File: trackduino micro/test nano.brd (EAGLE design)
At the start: 43.4 x 19.1 mm, 25 parts, among them IC2 74AHC1G125DBV, SW1 SPST_TACT-KMR2, U1 ATMEGA168MLF, X1 SMA-SMD, Y1 16MHZ

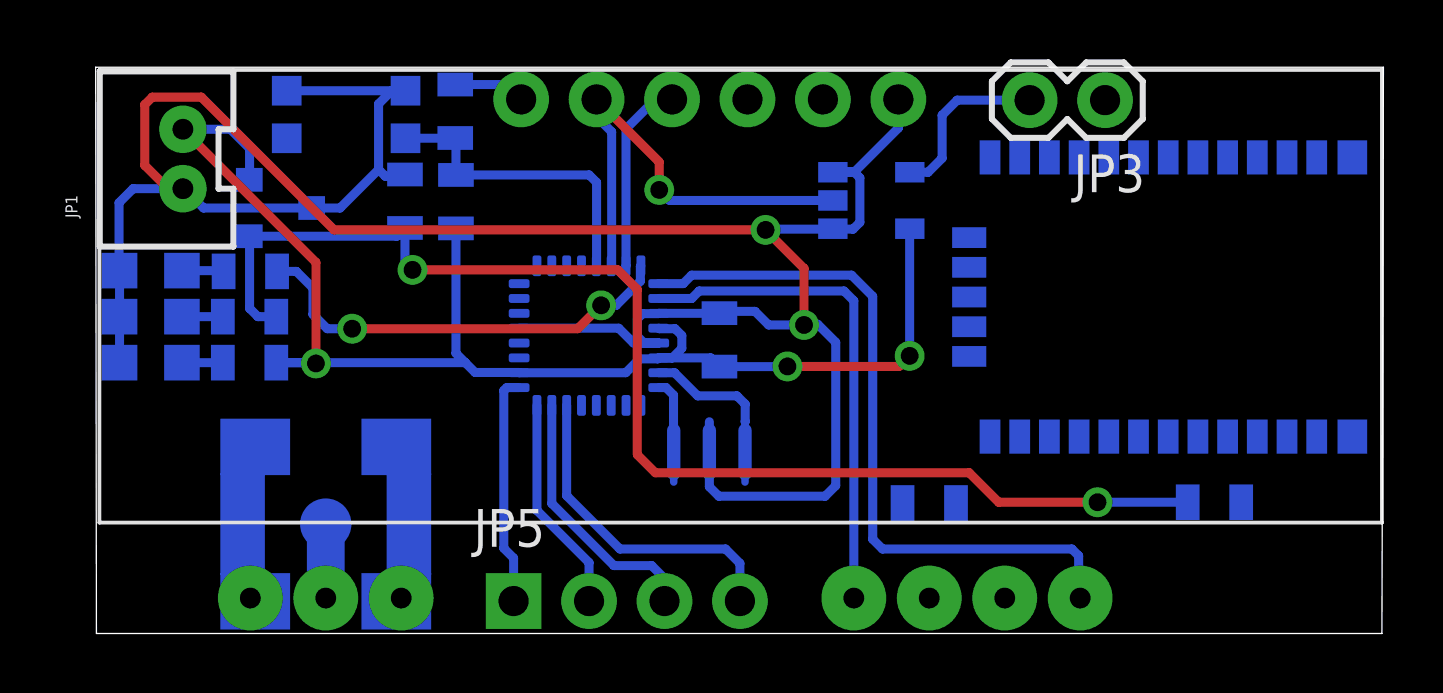
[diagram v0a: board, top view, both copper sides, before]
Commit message: minor fixes to smallest boards
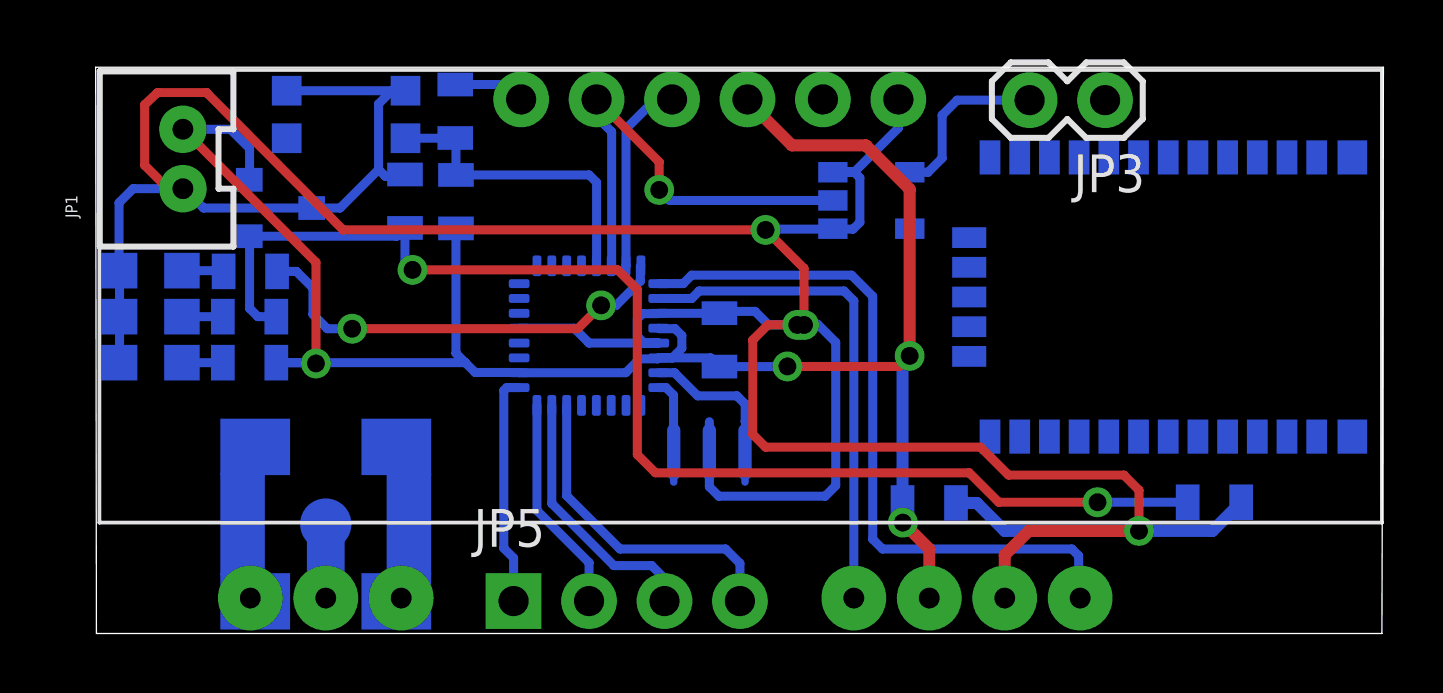
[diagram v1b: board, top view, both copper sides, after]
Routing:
- net GND: track 88.4 -> 125.2 mm, vias 2 -> 4
- net VCC: track 47.8 -> 68.7 mm, vias 3 -> 4
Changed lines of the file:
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@@
 <wire x1="76.8604" y1="71.0692" x2="76.1952" y2="71.0692" width="0.3048" layer="16"/>
 <wire x1="76.1952" y1="71.0692" x2="76.18" y2="71.0844" width="0.3048" layer="16"/>
-<wire x1="65.61656875" y1="67.734715625" x2="68.968084375" y2="67.734715625" width="0.3048" layer="16"/>
-<wire x1="68.968084375" y1="67.734715625" x2="69.469" y2="67.2338" width="0.3048" layer="16"/>
-<wire x1="69.469" y1="67.2338" x2="70.315653125" y2="67.2338" width="0.3048" layer="16"/>
+<wire x1="65.61656875" y1="67.734715625" x2="67.469484375" y2="67.734715625" width="0.3048" layer="16"/>
+<wire x1="67.469484375" y1="67.734715625" x2="67.9704" y2="67.2338" width="0.3048" layer="16"/>
+<wire x1="67.9704" y1="67.2338" x2="70.315653125" y2="67.2338" width="0.3048" layer="16"/>
 <wire x1="70.315653125" y1="67.2338" x2="70.31656875" y2="67.234715625" width="0.3048" layer="16"/>
 <wire x1="70.31656875" y1="67.234715625" x2="69.823684375" y2="67.234715625" width="0.3048" layer="16"/>
@@
 <wire x1="76.2762" y1="62.4332" x2="76.2762" y2="67.2592" width="0.3048" layer="16"/>
 <wire x1="76.2762" y1="67.2592" x2="75.6666" y2="67.8688" width="0.3048" layer="16"/>
-<wire x1="75.2094" y1="67.8434" x2="74.0156" y2="67.8434" width="0.3048" layer="16"/>
+<wire x1="75.2094" y1="67.8434" x2="74.9808" y2="67.8434" width="0.3048" layer="16"/>
+<wire x1="74.9808" y1="67.8434" x2="74.0156" y2="67.8434" width="0.3048" layer="16"/>
 <wire x1="74.0156" y1="67.8434" x2="73.5584" y2="68.3006" width="0.3048" layer="16"/>
 <wire x1="73.5584" y1="68.3006" x2="72.420778125" y2="68.3006" width="0.3048" layer="16"/>
@@
 <wire x1="73.9394" y1="71.0692" x2="73.914" y2="71.0438" width="0.3048" layer="16"/>
 <via x="73.914" y="71.0438" extent="1-16" drill="0.6" shape="square"/>
-<wire x1="73.914" y1="71.0438" x2="59.3852" y2="71.0438" width="0.3048" layer="1"/>
-<wire x1="59.3852" y1="71.0438" x2="54.9148" y2="75.5142" width="0.3048" layer="1"/>
-<wire x1="54.9148" y1="75.5142" x2="53.2638" y2="75.5142" width="0.3048" layer="1"/>
-<wire x1="53.2638" y1="75.5142" x2="53.0098" y2="75.2602" width="0.3048" layer="1"/>
+<wire x1="73.914" y1="71.0438" x2="59.69" y2="71.0438" width="0.3048" layer="1"/>
+<wire x1="59.69" y1="71.0438" x2="55.0926" y2="75.6666" width="0.3048" layer="1"/>
+<wire x1="55.0926" y1="75.6666" x2="53.4416" y2="75.6666" width="0.3048" layer="1"/>
+<wire x1="53.4416" y1="75.6666" x2="53.0098" y2="75.2602" width="0.3048" layer="1"/>
 <wire x1="53.0098" y1="75.2602" x2="53.0098" y2="73.2188" width="0.3048" layer="1"/>
 <wire x1="53.0098" y1="73.2188" x2="53.7972" y2="72.4314" width="0.3048" layer="1"/>
@@
 <wire x1="75.2094" y1="67.8434" x2="75.2094" y2="69.7484" width="0.3048" layer="1"/>
 <wire x1="75.2094" y1="69.7484" x2="73.914" y2="71.0438" width="0.3048" layer="1"/>
-<wire x1="81.9658" y1="58.6486" x2="89.927" y2="61.8744" width="0" layer="19" extent="16-16"/>
-<wire x1="80.3258" y1="61.849" x2="81.9658" y2="58.6486" width="0" layer="19" extent="16-16"/>
-<wire x1="76.2762" y1="62.4332" x2="80.3258" y2="61.849" width="0" layer="19" extent="16-16"/>
-<wire x1="56.7308" y1="63.7378" x2="52.163" y2="66.5734" width="0" layer="19" extent="16-16"/>
+<wire x1="80.3258" y1="61.849" x2="81.026" y2="61.849" width="0.4064" layer="16"/>
+<wire x1="81.026" y1="61.849" x2="81.9658" y2="60.9092" width="0.4064" layer="16"/>
+<wire x1="81.9658" y1="60.9092" x2="86.487" y2="60.9092" width="0.4064" layer="16"/>
+<wire x1="81.9658" y1="58.6486" x2="81.9658" y2="60.0964" width="0.4064" layer="1"/>
+<wire x1="81.9658" y1="60.0964" x2="82.7786" y2="60.9092" width="0.4064" layer="1"/>
+<wire x1="82.7786" y1="60.9092" x2="86.487" y2="60.9092" width="0.4064" layer="1"/>
+<via x="86.487" y="60.9092" extent="1-16" drill="0.6" shape="square"/>
+<wire x1="86.487" y1="60.9092" x2="88.9618" y2="60.9092" width="0.4064" layer="16"/>
+<wire x1="88.9618" y1="60.9092" x2="89.927" y2="61.8744" width="0.4064" layer="16"/>
+<via x="74.9808" y="67.8434" extent="1-16" drill="0.6" shape="square"/>
+<wire x1="74.9808" y1="67.8434" x2="73.9902" y2="67.8434" width="0.3048" layer="1"/>
+<wire x1="73.9902" y1="67.8434" x2="73.4822" y2="67.3354" width="0.3048" layer="1"/>
+<wire x1="73.4822" y1="67.3354" x2="73.4822" y2="64.1604" width="0.3048" layer="1"/>
+<wire x1="73.4822" y1="64.1604" x2="73.914" y2="63.7286" width="0.3048" layer="1"/>
+<wire x1="73.914" y1="63.7286" x2="81.153" y2="63.7286" width="0.3048" layer="1"/>
+<wire x1="81.153" y1="63.7286" x2="82.0928" y2="62.7888" width="0.3048" layer="1"/>
+<wire x1="82.0928" y1="62.7888" x2="85.979" y2="62.7888" width="0.3048" layer="1"/>
+<wire x1="85.979" y1="62.7888" x2="86.487" y2="62.2808" width="0.3048" layer="1"/>
+<wire x1="86.487" y1="62.2808" x2="86.487" y2="60.9092" width="0.3048" layer="1"/>
+<wire x1="61.9058" y1="61.1378" x2="61.4808" y2="63.7378" width="0" layer="19" extent="16-16"/>
+<wire x1="61.6458" y1="58.6486" x2="61.9058" y2="61.1378" width="0" layer="19" extent="16-16"/>
+<wire x1="61.4808" y1="58.5378" x2="61.6458" y2="58.6486" width="0" layer="19" extent="16-16"/>
+<wire x1="56.7308" y1="63.7378" x2="61.4808" y2="63.7378" width="0" layer="19" extent="16-16"/>
 <wire x1="56.3058" y1="61.1378" x2="56.7308" y2="63.7378" width="0" layer="19" extent="16-16"/>
 <wire x1="56.5658" y1="58.6486" x2="56.3058" y2="61.1378" width="0" layer="19" extent="16-16"/>
 <wire x1="56.7308" y1="58.5378" x2="56.5658" y2="58.6486" width="0" layer="19" extent="16-16"/>
-<wire x1="61.4808" y1="63.7378" x2="56.7308" y2="63.7378" width="0" layer="19" extent="16-16"/>
-<wire x1="61.9058" y1="61.1378" x2="61.4808" y2="63.7378" width="0" layer="19" extent="16-16"/>
-<wire x1="61.6458" y1="58.6486" x2="61.9058" y2="61.1378" width="0" layer="19" extent="16-16"/>
-<wire x1="61.4808" y1="58.5378" x2="61.6458" y2="58.6486" width="0" layer="19" extent="16-16"/>
+<wire x1="52.163" y1="66.5734" x2="56.7308" y2="63.7378" width="0" layer="19" extent="16-16"/>
 </signal>
 <signal name="VCC">
@@
 <wire x1="58.7756" y1="66.548" x2="58.7756" y2="69.9522" width="0.3048" layer="1"/>
 <wire x1="58.7756" y1="69.9522" x2="54.2964" y2="74.4314" width="0.3048" layer="1"/>
-<wire x1="73.3044" y1="75.438" x2="78.77" y2="71.0844" width="0" layer="19" extent="16-16"/>
-<wire x1="78.5258" y1="61.849" x2="72.360990625" y2="66.4408125" width="0" layer="19" extent="16-16"/>
-<wire x1="79.4258" y1="58.6486" x2="78.5258" y2="61.849" width="0" layer="19" extent="16-16"/>
 <wire x1="72.360990625" y1="66.4408125" x2="74.6450125" y2="66.4408125" width="0.3048" layer="16"/>
 <wire x1="74.6450125" y1="66.4408125" x2="74.6506" y2="66.4464" width="0.3048" layer="16"/>
@@
 <wire x1="78.7654" y1="66.802" x2="78.7654" y2="71.0798" width="0.3048" layer="16"/>
 <wire x1="78.7654" y1="71.0798" x2="78.77" y2="71.0844" width="0.3048" layer="16"/>
+<wire x1="73.3044" y1="75.438" x2="73.3044" y2="75.3872" width="0.4064" layer="1"/>
+<wire x1="73.3044" y1="75.3872" x2="74.803" y2="73.8886" width="0.4064" layer="1"/>
+<wire x1="74.803" y1="73.8886" x2="77.2922" y2="73.8886" width="0.4064" layer="1"/>
+<wire x1="77.2922" y1="73.8886" x2="78.7654" y2="72.4154" width="0.4064" layer="1"/>
+<wire x1="78.7654" y1="72.4154" x2="78.7654" y2="66.802" width="0.4064" layer="1"/>
+<wire x1="79.4258" y1="58.6486" x2="79.4258" y2="60.2996" width="0.4064" layer="1"/>
+<wire x1="79.4258" y1="60.2996" x2="78.5368" y2="61.1886" width="0.4064" layer="1"/>
+<via x="78.5368" y="61.1886" extent="1-16" drill="0.6" shape="square"/>
+<wire x1="78.5368" y1="61.1886" x2="78.5368" y2="61.838" width="0.4064" layer="16"/>
+<wire x1="78.5368" y1="61.838" x2="78.5258" y2="61.849" width="0.4064" layer="16"/>
+<wire x1="78.5258" y1="61.849" x2="78.5258" y2="66.5624" width="0.4064" layer="16"/>
+<wire x1="78.5258" y1="66.5624" x2="78.7654" y2="66.802" width="0.4064" layer="16"/>
 </signal>
 <signal name="TX-3V3">
@@
 <contactref element="SW1" pad="1"/>
 <contactref element="SW1" pad="3"/>
-<wire x1="57.7916" y1="74.13" x2="61.7916" y2="74.13" width="0" layer="19" extent="16-16"/>
 <wire x1="61.7916" y1="74.13" x2="63.457065625" y2="74.13" width="0.3048" layer="16"/>
 <wire x1="63.457065625" y1="74.13" x2="63.464825" y2="74.137759375" width="0.3048" layer="16"/>
@@
 <wire x1="68.2244" y1="72.644" x2="68.2244" y2="69.842546875" width="0.3048" layer="16"/>
 <wire x1="68.2244" y1="69.842546875" x2="68.21656875" y2="69.834715625" width="0.3048" layer="16"/>
+<wire x1="57.7916" y1="74.13" x2="61.7916" y2="74.13" width="0" layer="19" extent="16-16"/>
 </signal>
 <signal name="RXO">
